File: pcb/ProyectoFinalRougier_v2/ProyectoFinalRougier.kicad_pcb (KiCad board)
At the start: 2 copper layers, 40 x 35 mm, 28 parts, among them J1 Screw_Terminal_01x02, J2 Screw_Terminal_01x02, J3 Conn_01x06, U1 AD8495, U2 AD8495, U3 TL431DBZ, U4 TL431DBZ

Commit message: Se agregan etiquetas y comentarios a los dos PCBs
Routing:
- net GND: track 128.6 -> 130.0 mm
- net Net-(J3-Pad3): track 37.3 -> 38.2 mm
- net Net-(J2-Pad1): track 22.0 -> 21.1 mm
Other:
- net class Default: clearance 0.7 -> 0.8
- rule trace_clearance: 0.7 -> 0.8
- board text added: "13-10-21"
- board text added: "GRILLAS BORDE PCB: Grilla 2.50 mm MARGEN: Grilla 0.5 mm POSICIONAMIENTO: Grila 1.00 mm RUTEO ANCHO DE PISTA GENERAL 0.80 mm - Grilla 1.00 mm ANCHO DE PISTA AD8495 0.30 mm - Grilla 0.25 mm MARGEN GENERAL 0.8 mm (Default) AD8495 0.2 mm FABRICANTE Se toma en cuenta la información de fabricación de Ernesto Mayer Carlos Pellegrini 1257/61 (B1604ASG) Florida Oeste Buenos Aires – Argentina - Tel.: +5411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"
- board text added: "IND. ARG."
- board text added: "Réplica AD8495"
- board text added: "Terminación Superficial HASL (SnPb)"
- board text added: "Ver 1.0"

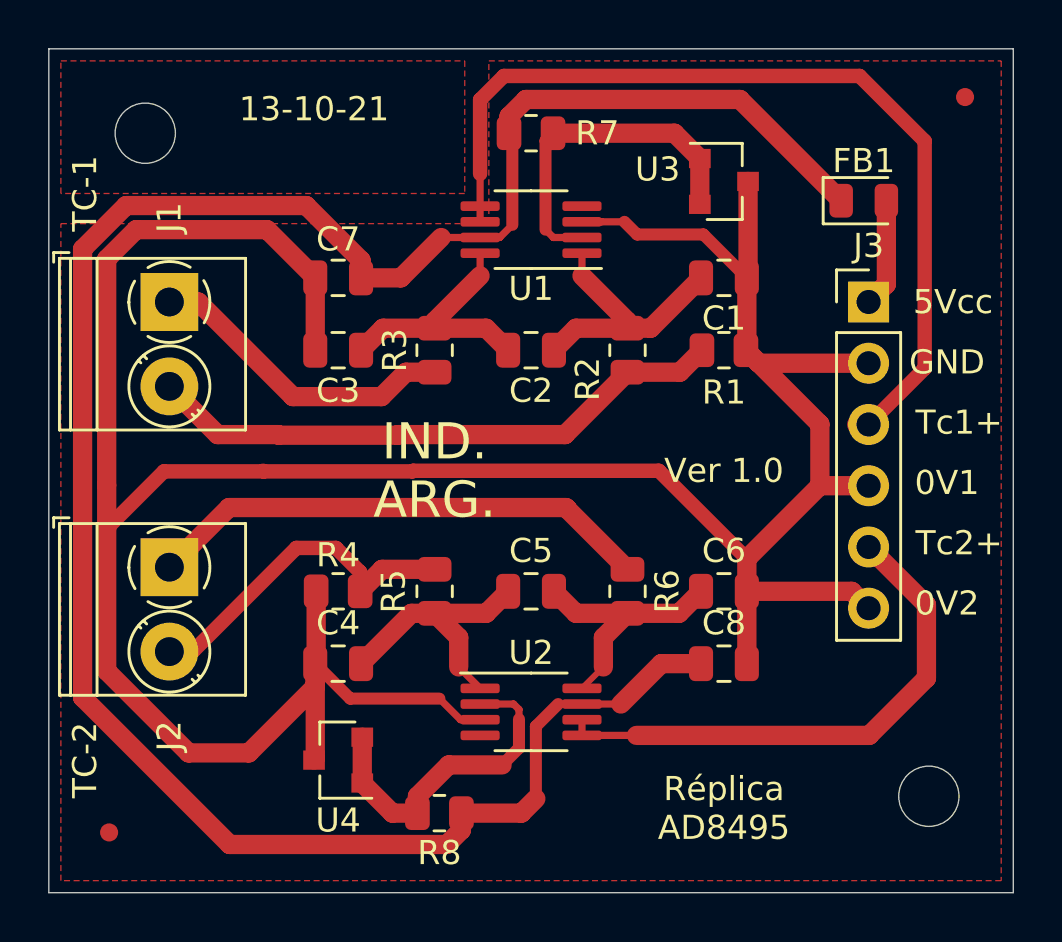
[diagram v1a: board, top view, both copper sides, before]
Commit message: Ajuste del Margen, se aumentó el menor margen que limita el AD8495
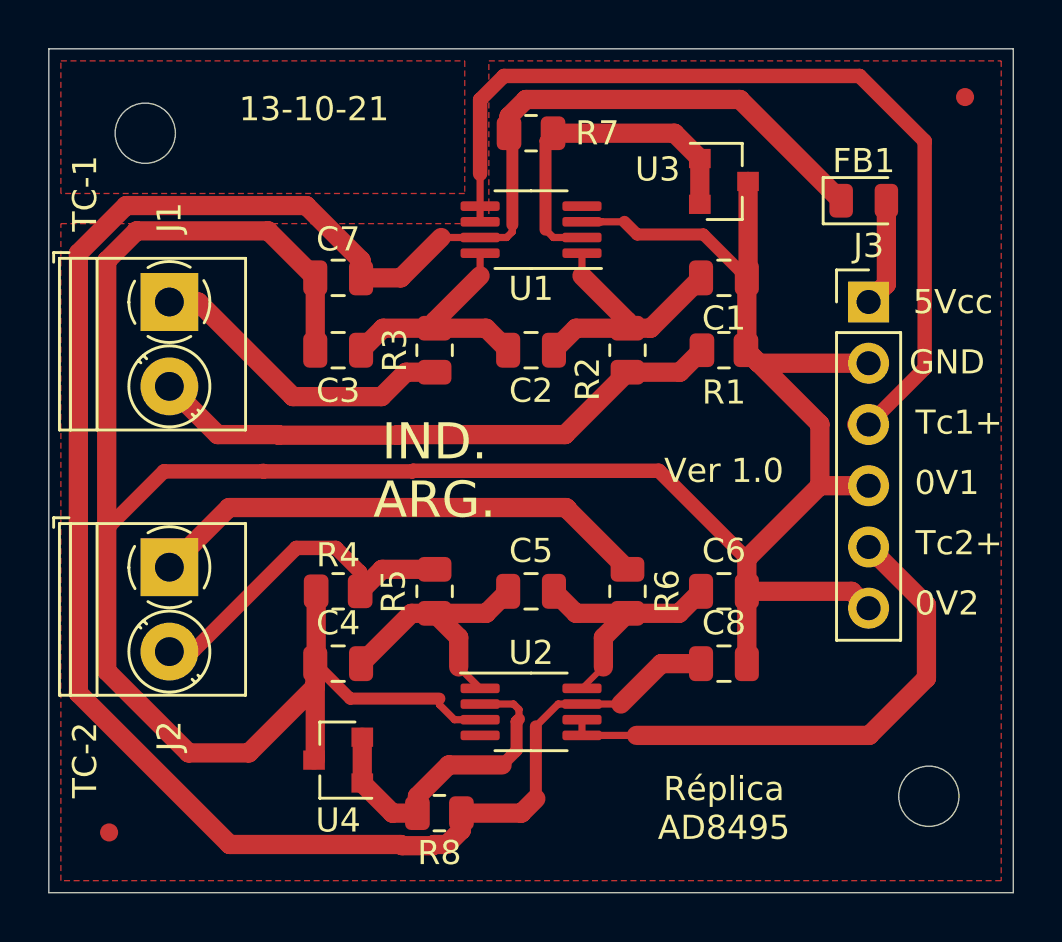
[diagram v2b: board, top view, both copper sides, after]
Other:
- net class AD8495: clearance 0.2 -> 0.25
- rule trace_min: 0.2 -> 0.25
